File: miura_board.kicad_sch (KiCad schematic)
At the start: 41 parts, among them J1 Screw_Terminal_01x02, J2 Screw_Terminal_01x02, J3 Screw_Terminal_01x02, J4 Conn_01x04_Male, J5 Screw_Terminal_01x02, J6 Screw_Terminal_01x02, J7 Screw_Terminal_01x02, J8 Screw_Terminal_01x02, SW1 SW_Push, SW2 SW_Push, U1 ESP32-WROOM, U2 W25Q32JVSS, U3 DRV8833PW, U4 DRV8833PW, U5 AMS1117, U6 MPU-6050, U7 L7806, U8 DRV8833PW

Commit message: lol
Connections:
- net MOTOR_A11_IN: now also U1.24 (IO2); no longer U1.13 (IO14)
- net MOTOR_A12_IN: now also U1.23 (IO15); no longer U1.12 (IO27)
- net MOTOR_A21_IN: now also U1.6 (IO34); no longer U1.9 (IO33), U8.16 (AIN1)
- net MOTOR_A22_IN: now also U1.7 (IO35); no longer U1.8 (IO32), U8.15 (AIN2)
- net MOTOR_B11_IN: now also U1.14 (IO12); no longer U1.11 (IO26)
- net MOTOR_B12_IN: now also U1.16 (IO13); no longer U1.10 (IO25)
- net MOTOR_B21_IN: now also U1.9 (IO33); no longer U1.7 (IO35), U8.9 (BIN1)
- net MOTOR_B22_IN: now also U1.8 (IO32); no longer U1.6 (IO34), U8.10 (BIN2)
- net at U3.2 (AOUT1): now also J6.2 (Pin_2); no longer J6.1 (Pin_1)
- net at U3.4 (AOUT2): now also J6.1 (Pin_1); no longer J6.2 (Pin_2)
- net at U3.5 (BOUT2): now also J2.1 (Pin_1); no longer J2.2 (Pin_2)
- net at U3.7 (BOUT1): now also J2.2 (Pin_2); no longer J2.1 (Pin_1)
- new net MOTOR_A31_IN: U1.10 (IO25), U8.16 (AIN1)
- new net MOTOR_A32_IN: U1.11 (IO26), U8.15 (AIN2)
- new net MOTOR_B31_IN: U1.12 (IO27), U8.9 (BIN1)
- new net MOTOR_B32_IN: U1.13 (IO14), U8.10 (BIN2)
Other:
- moved on the sheet: J2, J6

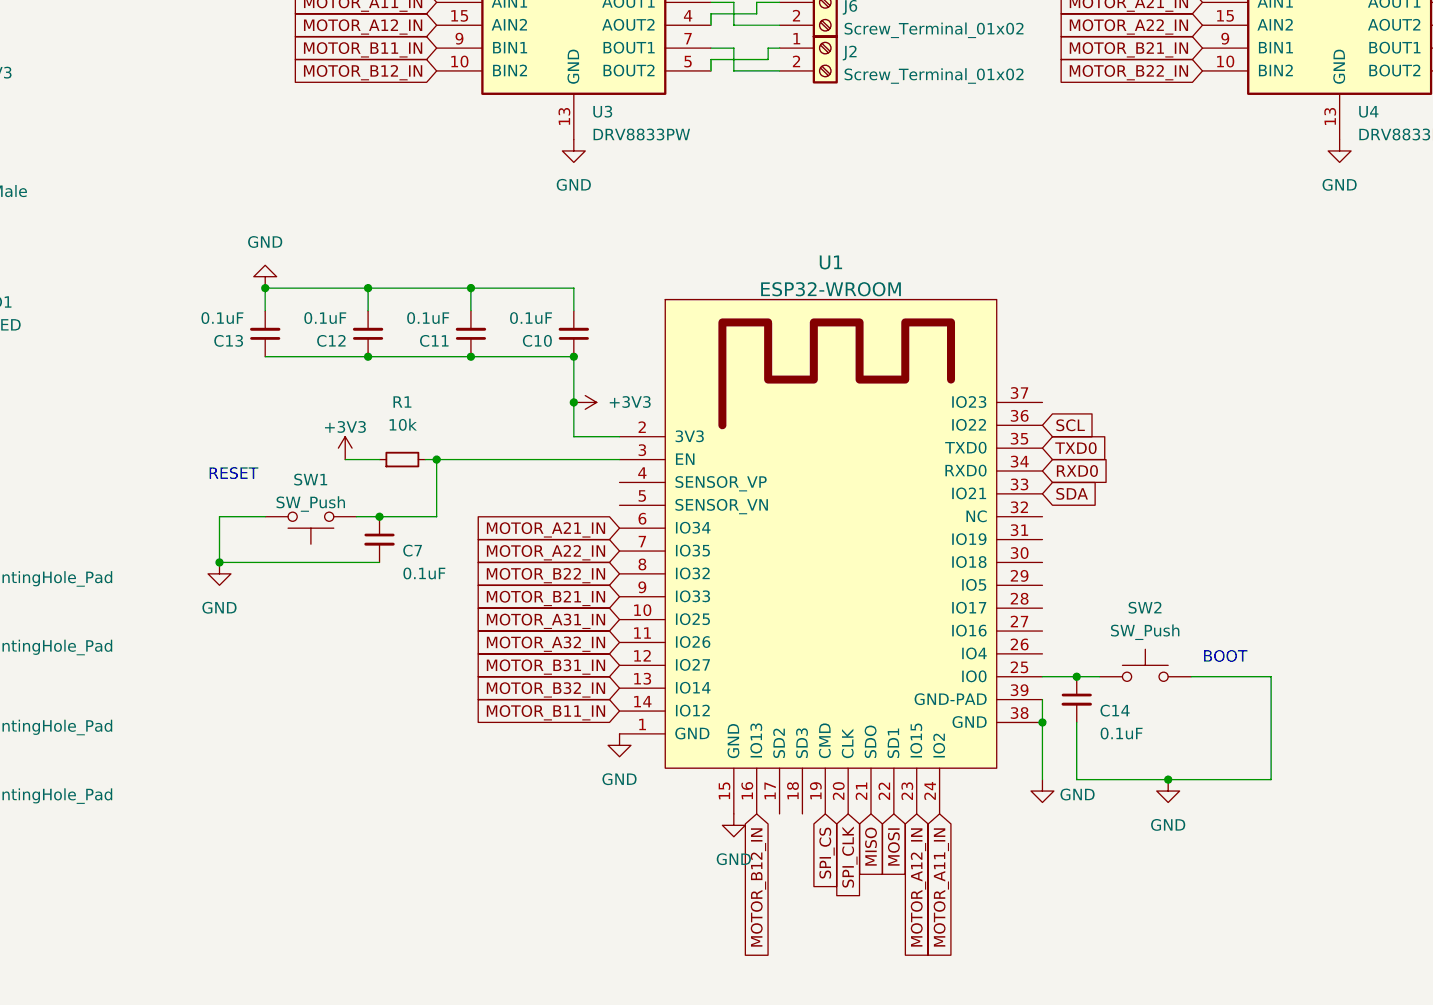
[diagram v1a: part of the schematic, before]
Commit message: Added more silk
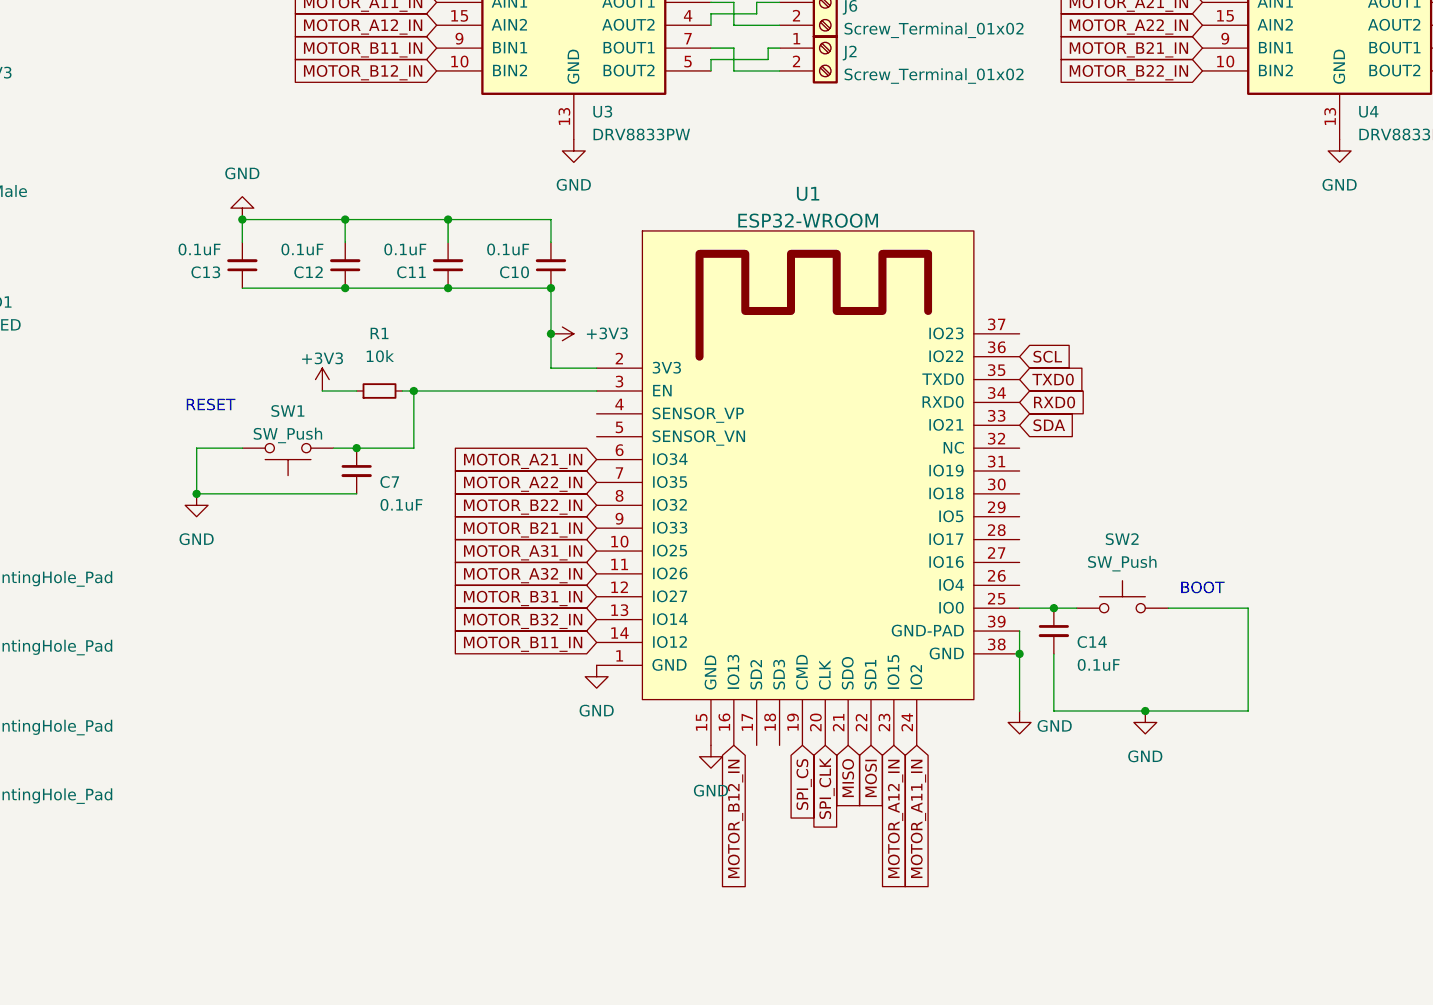
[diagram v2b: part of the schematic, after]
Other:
- moved on the sheet: C10, C11, C12, C13, C14, C7, R1, SW1, SW2, U1

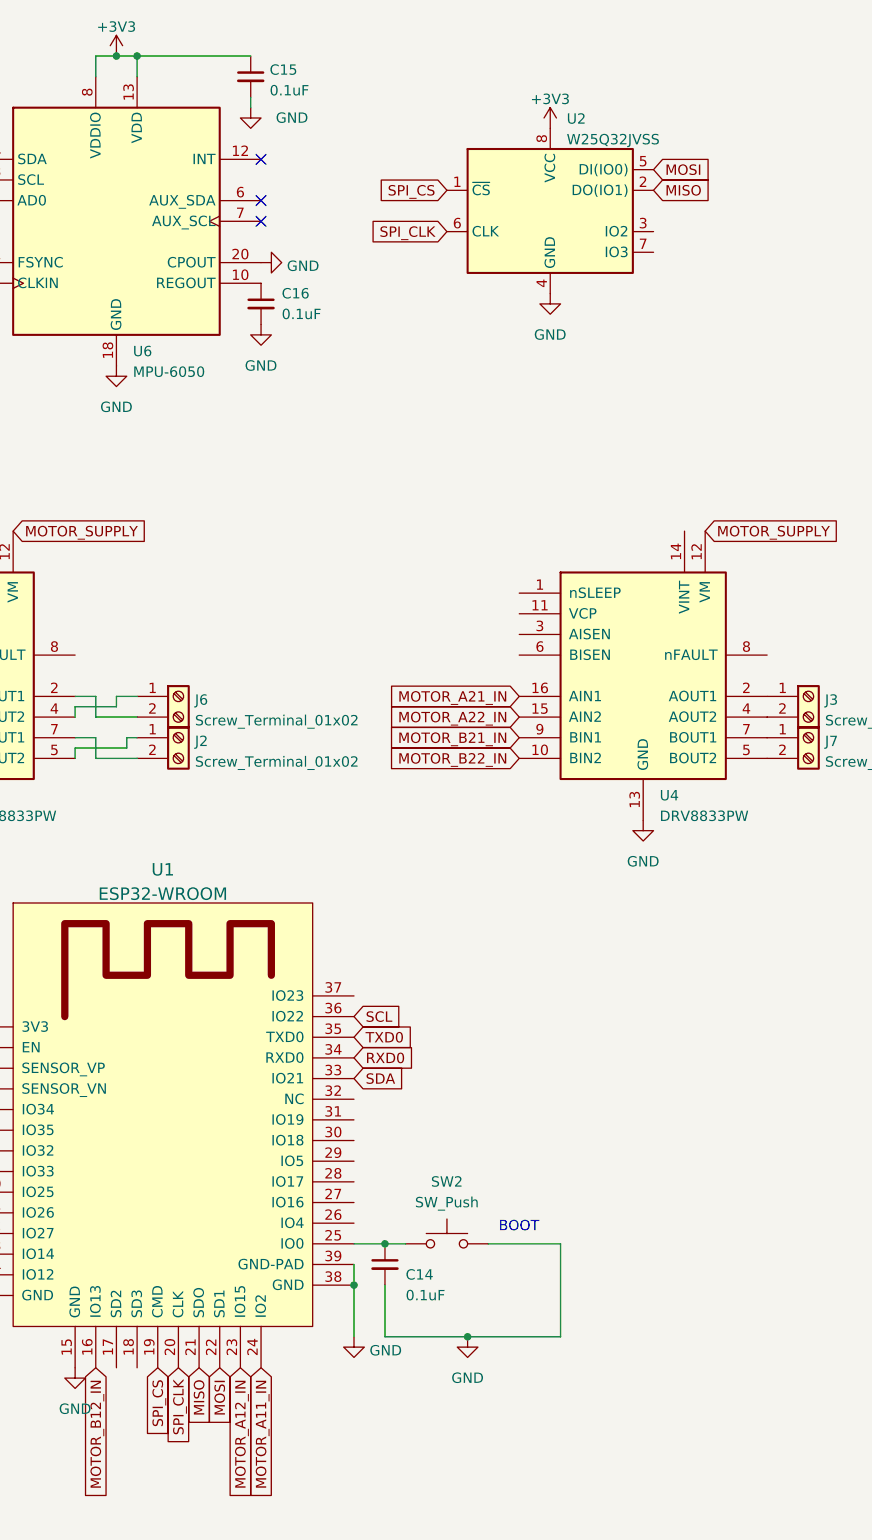
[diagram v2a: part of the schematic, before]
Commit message: Ordered board, removed SPI flash
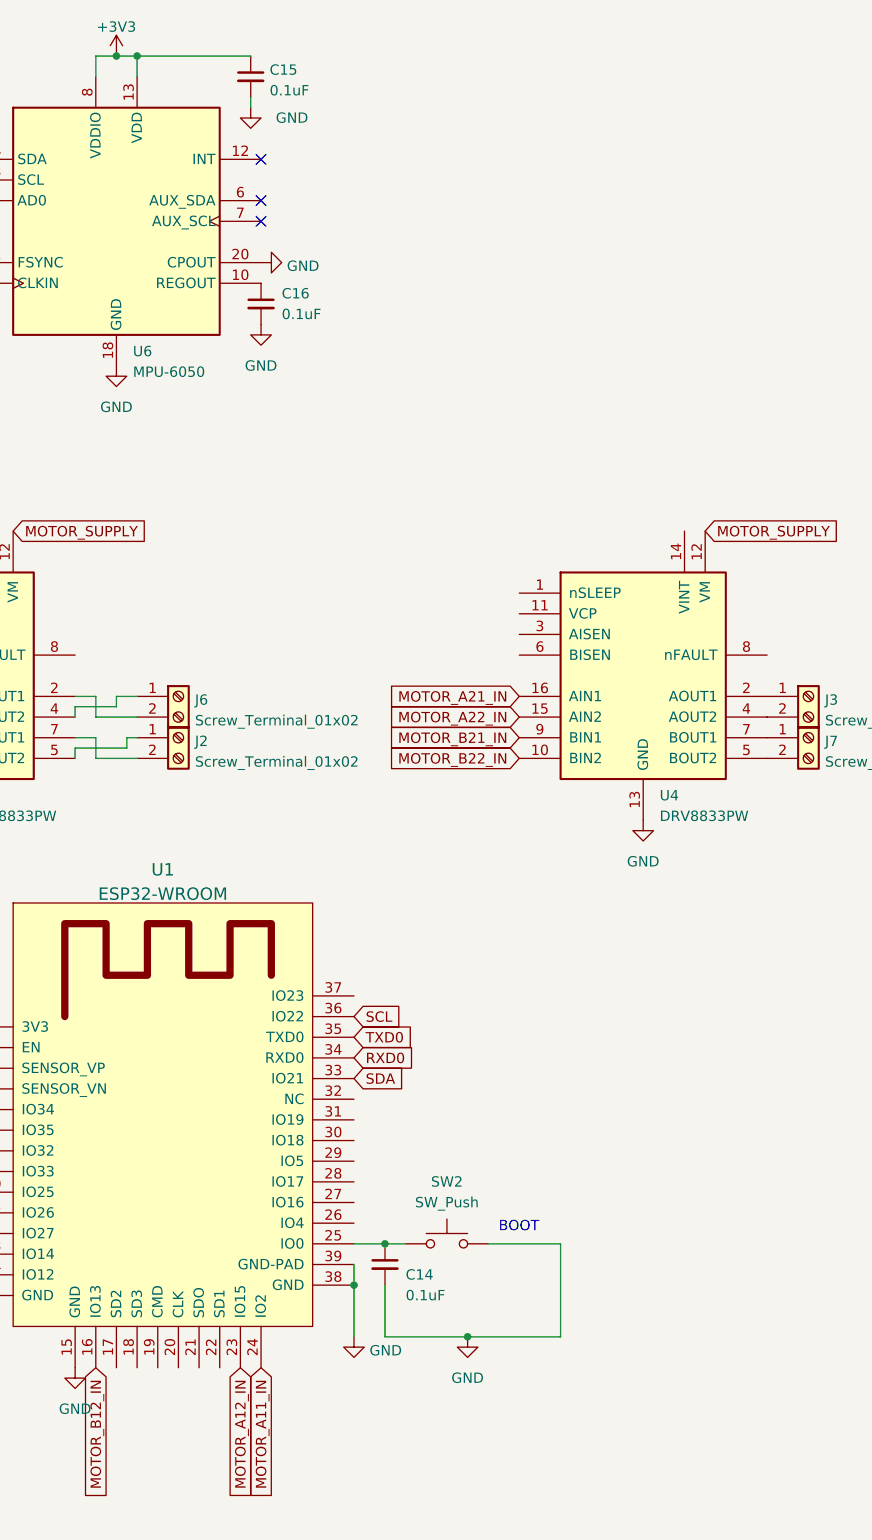
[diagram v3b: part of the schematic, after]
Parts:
- removed U2: W25Q32JVSS, Package_SO:SOIC-8_5.23x5.23mm_P1.27mm, symbol Memory_Flash:W25Q32JVSS
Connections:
- net MISO: no longer names the net of U1.21 (SDO)
- net MOSI: no longer names the net of U1.22 (SD1)
- net SPI_CLK: no longer names the net of U1.20 (CLK)
- net SPI_CS: no longer names the net of U1.19 (CMD)
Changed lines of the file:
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@@
-    )
-  )
-  (global_label "MISO" (shape input) (at 121.92 179.07 270) (fields_autoplaced)
-    (effects (font (size 1.27 1.27)) (justify right))
-    (property "Intersheet References" "${INTERSHEET_REFS}" (id 0) (at 121.8406 186.0793 90)
-      (effects (font (size 1.27 1.27)) (justify right) hide)
-    )
-  )
-  (global_label "SPI_CS" (shape input) (at 152.4 34.29 180) (fields_autoplaced)
-    (effects (font (size 1.27 1.27)) (justify right))
-    (property "Intersheet References" "${INTERSHEET_REFS}" (id 0) (at 143.4555 34.2106 0)
-      (effects (font (size 1.27 1.27)) (justify right) hide)
     )
   )
@@
     )
   )
-  (global_label "SPI_CLK" (shape input) (at 119.38 179.07 270) (fields_autoplaced)
-    (effects (font (size 1.27 1.27)) (justify right))
-    (property "Intersheet References" "${INTERSHEET_REFS}" (id 0) (at 119.3006 189.1031 90)
-      (effects (font (size 1.27 1.27)) (justify right) hide)
-    )
-  )
   (global_label "MOTOR_A31_IN" (shape input) (at 224.79 129.54 180) (fields_autoplaced)
     (effects (font (size 1.27 1.27)) (justify right))
@@
     )
   )
-  (global_label "SPI_CS" (shape input) (at 116.84 179.07 270) (fields_autoplaced)
-    (effects (font (size 1.27 1.27)) (justify right))
-    (property "Intersheet References" "${INTERSHEET_REFS}" (id 0) (at 116.7606 188.0145 90)
-      (effects (font (size 1.27 1.27)) (justify right) hide)
-    )
-  )
-  (global_label "MISO" (shape input) (at 177.8 34.29 0) (fields_autoplaced)
-    (effects (font (size 1.27 1.27)) (justify left))
-    (property "Intersheet References" "${INTERSHEET_REFS}" (id 0) (at 184.8093 34.3694 0)
-      (effects (font (size 1.27 1.27)) (justify left) hide)
-    )
-  )
   (global_label "MOTOR_B12_IN" (shape input) (at 76.2 104.14 180) (fields_autoplaced)
     (effects (font (size 1.27 1.27)) (justify right))
@@
     )
   )
-  (global_label "MOSI" (shape input) (at 124.46 179.07 270) (fields_autoplaced)
-    (effects (font (size 1.27 1.27)) (justify right))
-    (property "Intersheet References" "${INTERSHEET_REFS}" (id 0) (at 124.3806 186.0793 90)
-      (effects (font (size 1.27 1.27)) (justify right) hide)
-    )
-  )
   (global_label "MOTOR_A12_IN" (shape input) (at 76.2 99.06 180) (fields_autoplaced)
     (effects (font (size 1.27 1.27)) (justify right))
@@
     )
   )
-  (global_label "SPI_CLK" (shape input) (at 152.4 39.37 180) (fields_autoplaced)
-    (effects (font (size 1.27 1.27)) (justify right))
-    (property "Intersheet References" "${INTERSHEET_REFS}" (id 0) (at 142.3669 39.2906 0)
-      (effects (font (size 1.27 1.27)) (justify right) hide)
-    )
-  )
   (global_label "VBAT" (shape input) (at 20.32 31.75 0) (fields_autoplaced)
     (effects (font (size 1.27 1.27)) (justify left))
@@
     (property "Intersheet References" "${INTERSHEET_REFS}" (id 0) (at 77.8388 149.7806 0)
       (effects (font (size 1.27 1.27)) (justify right) hide)
-    )
-  )
-  (global_label "MOSI" (shape input) (at 177.8 31.75 0) (fields_autoplaced)
-    (effects (font (size 1.27 1.27)) (justify left))
-    (property "Intersheet References" "${INTERSHEET_REFS}" (id 0) (at 184.8093 31.8294 0)
-      (effects (font (size 1.27 1.27)) (justify left) hide)
     )
   )
@@
     (pin "1")
   )
-  (symbol (lib_id "Memory_Flash:W25Q32JVSS") (at 165.1 36.83 0) (unit 1)
-    (in_bom yes) (on_board yes) (fields_autoplaced)
-    (property "Reference" "U2" (id 0) (at 167.1194 25.5102 0)
-      (effects (font (size 1.27 1.27)) (justify left))
-    )
-    (property "Value" "W25Q32JVSS" (id 1) (at 167.1194 28.0471 0)
-      (effects (font (size 1.27 1.27)) (justify left))
-    )
-    (property "Footprint" "Package_SO:SOIC-8_5.23x5.23mm_P1.27mm" (id 2) (at 165.1 36.83 0)
-      (effects (font (size 1.27 1.27)) hide)
-    )
-    (property "Datasheet" "http://www.winbond.com/resource-files/w25q32jv%20revg%2003272018%20plus.pdf" (id 3) (at 165.1 36.83 0)
-      (effects (font (size 1.27 1.27)) hide)
-    )
-    (pin "1")
-    (pin "2")
-    (pin "3")
-    (pin "4")
-    (pin "5")
-    (pin "6")
-    (pin "7")
-    (pin "8")
-  )
   (symbol (lib_id "Device:C_Small") (at 31.75 40.64 0) (unit 1)
     (in_bom yes) (on_board yes) (fields_autoplaced)
@@
     (pin "2")
   )
-  (symbol (lib_id "power:+3V3") (at 165.1 26.67 0) (unit 1)
-    (in_bom yes) (on_board yes) (fields_autoplaced)
-    (property "Reference" "#PWR0106" (id 0) (at 165.1 30.48 0)
-      (effects (font (size 1.27 1.27)) hide)
-    )
-    (property "Value" "+3V3" (id 1) (at 165.1 23.0942 0))
-    (property "Footprint" "" (id 2) (at 165.1 26.67 0)
-      (effects (font (size 1.27 1.27)) hide)
-    )
-    (property "Datasheet" "" (id 3) (at 165.1 26.67 0)
-      (effects (font (size 1.27 1.27)) hide)
-    )
-    (pin "1")
-  )
   (symbol (lib_id "power:GND") (at 154.94 175.26 0) (unit 1)
     (in_bom yes) (on_board yes) (fields_autoplaced)
@@
     (pin "1")
   )
-  (symbol (lib_id "power:GND") (at 165.1 46.99 0) (unit 1)
-    (in_bom yes) (on_board yes) (fields_autoplaced)
-    (property "Reference" "#PWR0107" (id 0) (at 165.1 53.34 0)
-      (effects (font (size 1.27 1.27)) hide)
-    )
-    (property "Value" "GND" (id 1) (at 165.1 52.07 0))
-    (property "Footprint" "" (id 2) (at 165.1 46.99 0)
-      (effects (font (size 1.27 1.27)) hide)
-    )
-    (property "Datasheet" "" (id 3) (at 165.1 46.99 0)
-      (effects (font (size 1.27 1.27)) hide)
-    )
-    (pin "1")
-  )
   (symbol (lib_id "Device:C_Small") (at 128.27 20.32 0) (unit 1)
     (in_bom yes) (on_board yes) (fields_autoplaced)
@@
       (reference "#PWR0105") (unit 1) (value "GND") (footprint "")
     )
-    (path "/d543c5b5-ea2c-4e29-af76-04af2da6ec14"
-      (reference "#PWR0106") (unit 1) (value "+3V3") (footprint "")
-    )
-    (path "/f57cccfc-7941-46d3-bdc7-53a9551c005d"
-      (reference "#PWR0107") (unit 1) (value "GND") (footprint "")
-    )
     (path "/b7b3ed82-23ca-412e-9deb-5cde18dd9e4f"
       (reference "#PWR0108") (unit 1) (value "GND") (footprint "")
@@
       (reference "U1") (unit 1) (value "ESP32-WROOM") (footprint "ESP32-footprints-Lib:ESP32-WROOM")
     )
-    (path "/777f729c-c6dd-4407-b25c-a12ee12fedf3"
-      (reference "U2") (unit 1) (value "W25Q32JVSS") (footprint "Package_SO:SOIC-8_5.23x5.23mm_P1.27mm")
-    )
     (path "/723fb764-14ee-4461-b800-e4d673c3e301"

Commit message: Working motor controller
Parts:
- removed D1: LED, LED_SMD:LED_0603_1608Metric, symbol Device:LED
- removed R7: 10k, Resistor_SMD:R_0603_1608Metric_Pad0.98x0.95mm_HandSolder, symbol Device:R_Small
- added C17, C19, C21: 0.1uF, Capacitor_SMD:C_0603_1608Metric, symbol Device:C_Small
- added C18, C20, C22: 2.2uF, Capacitor_SMD:C_0603_1608Metric, symbol Device:C_Small
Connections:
- net +3V3: now also U3.1 (nSLEEP), U4.1 (nSLEEP), U8.1 (nSLEEP)
- net GND: now also U3.3 (AISEN), U3.6 (BISEN), U4.3 (AISEN), U4.6 (BISEN), U8.3 (AISEN), U8.6 (BISEN), C18.1, C20.1, C22.1
- net MOTOR_SUPPLY: now also C17.1, C19.1, C21.1
- net at U3.11 (VCP): now also C17.2
- net at U3.14 (VINT): now also C18.2
- net at U4.11 (VCP): now also C19.2
- net at U4.14 (VINT): now also C20.2
- net at U8.11 (VCP): now also C21.2
- net at U8.14 (VINT): now also C22.2
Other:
- moved on the sheet: C15, C16, C2, C3, C5, C6, J2, J3, J5, J6, J7, U3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

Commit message: new board design
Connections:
- net MOTOR_A21_IN: now also U1.7 (IO35), U4.10 (BIN2); no longer U1.6 (IO34), U4.16 (AIN1)
- net MOTOR_A22_IN: now also U1.6 (IO34), U4.9 (BIN1); no longer U1.7 (IO35), U4.15 (AIN2)
- net MOTOR_B21_IN: now also U4.16 (AIN1); no longer U4.9 (BIN1)
- net MOTOR_B22_IN: now also U4.15 (AIN2); no longer U4.10 (BIN2)
- net IO32: now reaches J3.1 (Pin_1)
- net IO32: now also U4.4 (AOUT2); no longer U4.2 (AOUT1)
- net IO33: now reaches J3.2 (Pin_2)
- net IO33: now also U4.2 (AOUT1); no longer U4.4 (AOUT2)
- net IO25: now reaches U8.2 (AOUT1)
- net IO25: now also J1.2 (Pin_2); no longer J1.1 (Pin_1)
- net IO26: now reaches U8.4 (AOUT2)
- net IO26: now also J1.1 (Pin_1); no longer J1.2 (Pin_2)
- net IO13: now reaches J6.2 (Pin_2)
- net IO13: now also U3.5 (BOUT2); no longer U3.2 (AOUT1)
- net IO12: now reaches J6.1 (Pin_1)
- net IO12: now also U3.7 (BOUT1); no longer U3.4 (AOUT2)
- net IO15: now reaches J2.1 (Pin_1)
- net IO15: now also U3.4 (AOUT2); no longer U3.5 (BOUT2)
- net IO2: now reaches J2.2 (Pin_2)
- net IO2: now also U3.2 (AOUT1); no longer U3.7 (BOUT1)
- net IO35: now reaches J7.2 (Pin_2), U4.5 (BOUT2)
- net IO34: now reaches J7.1 (Pin_1), U4.7 (BOUT1)
- net IO14: now reaches U8.5 (BOUT2)
- net IO14: now also J8.1 (Pin_1); no longer J8.2 (Pin_2)
- net IO27: now reaches U8.7 (BOUT1)
- net IO27: now also J8.2 (Pin_2); no longer J8.1 (Pin_1)
- no-connect marks 5 -> 21
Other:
- moved on the sheet: C21, C22, J1, J2, J3, J6, J7, J8, U8
